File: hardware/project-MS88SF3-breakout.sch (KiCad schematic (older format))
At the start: 27 parts, among them J1 Conn_02x05_Odd_Even, J2 S2B-PH-SM4-TB(LF)(SN), J3 USB4105-GF-A, J4 Conn_01x12_Male, J5 Conn_01x16_Male, U1 MS88SF3

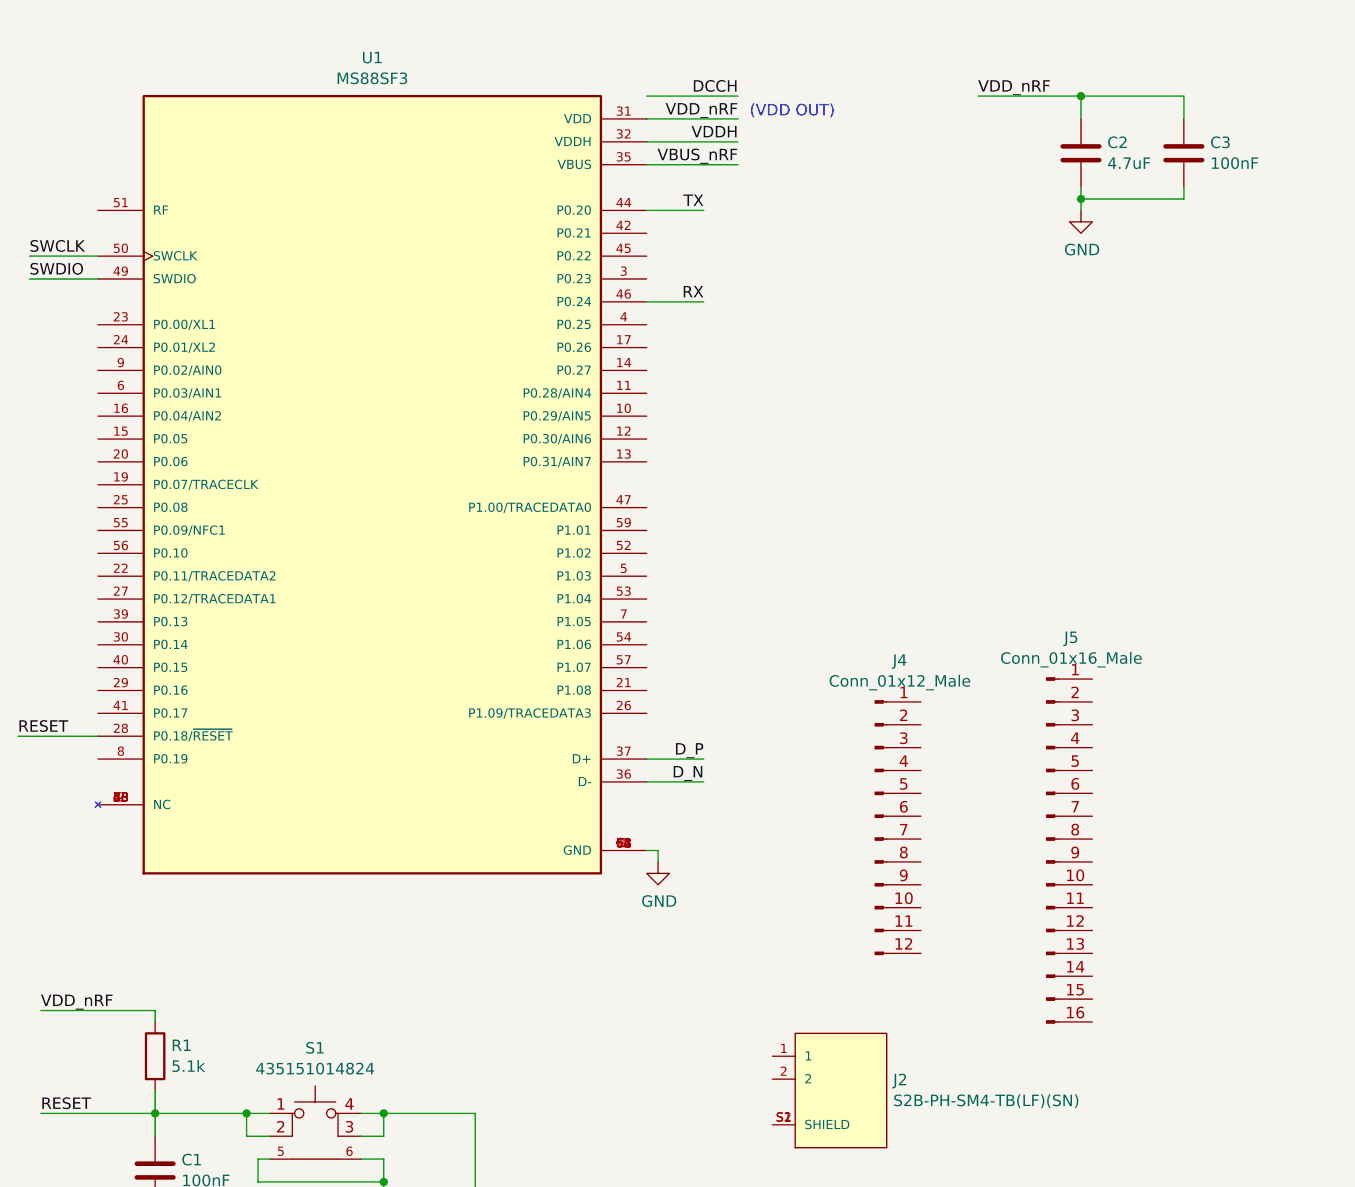
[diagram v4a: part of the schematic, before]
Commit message: Change the MS88SF3 module to the nRF52840
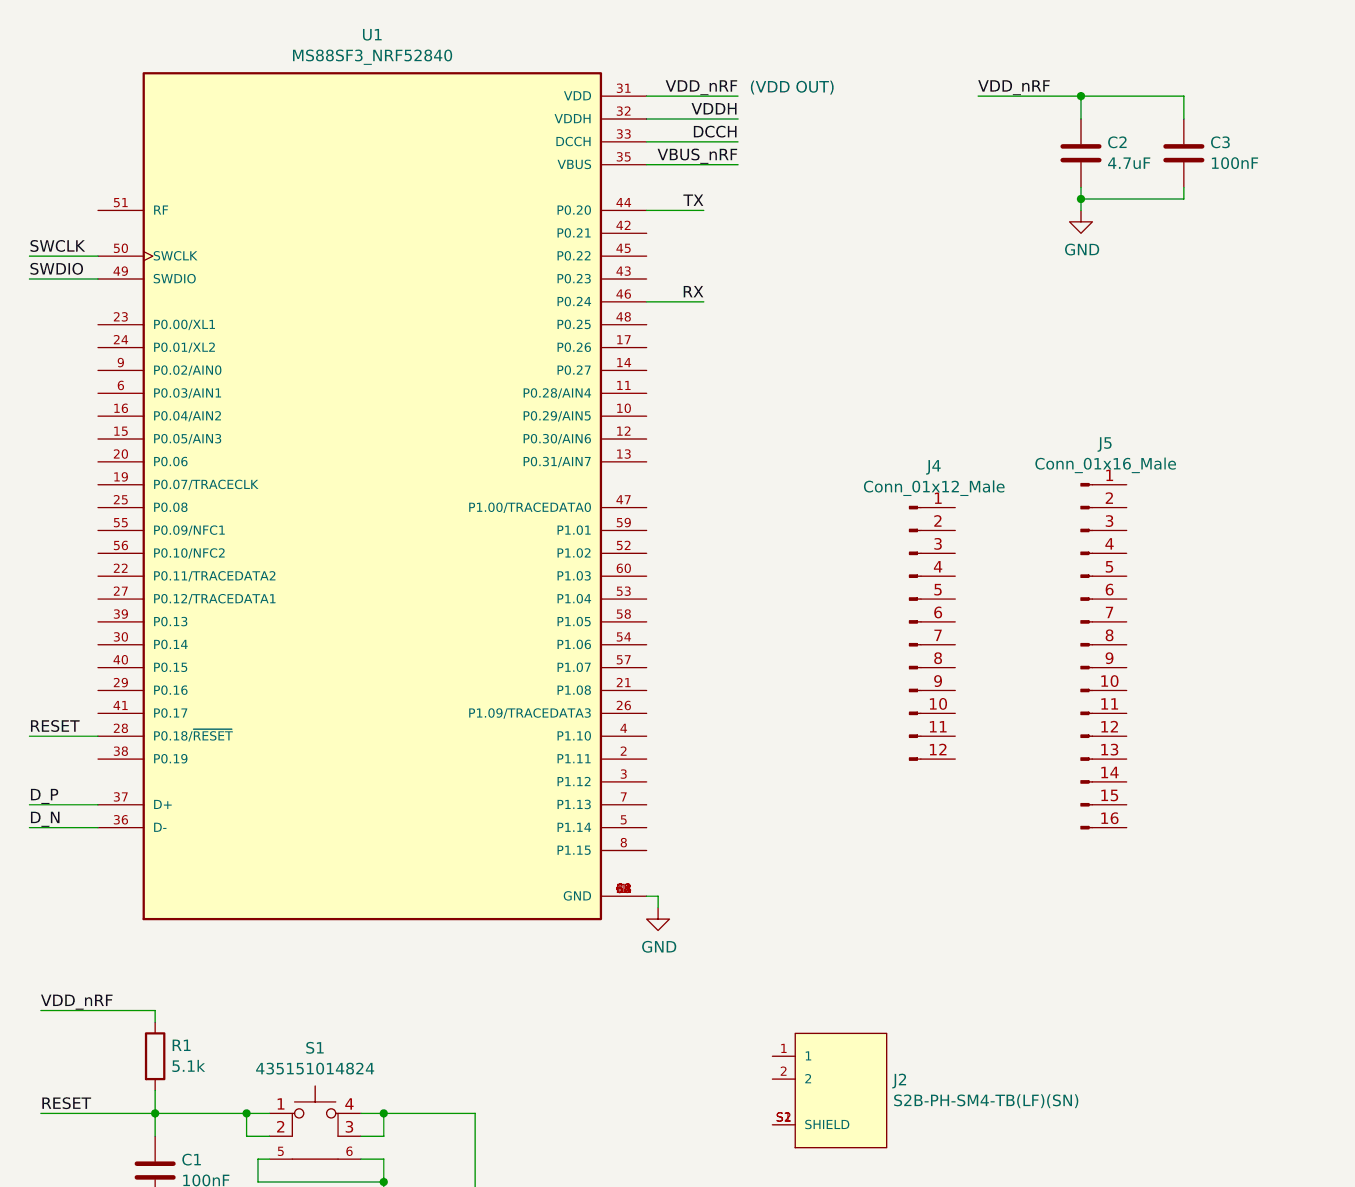
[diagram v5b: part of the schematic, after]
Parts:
- removed U1: MS88SF3, MODULE_MS88SF3, symbol MS88SF3:MS88SF3
- added U1: MS88SF3_NRF52840, MODULE_MS88SF3_NRF52840, symbol MS88SF3_NRF52840:MS88SF3_NRF52840
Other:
- moved on the sheet: J4, J5
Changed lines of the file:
@@
 $EndDescr
-$Comp
-L MS88SF3:MS88SF3 U1
-U 1 1 62BF0ECE
-P 2700 2850
-F 0 "U1" H 2700 4717 50  0000 C CNN
-F 1 "MS88SF3" H 2700 4626 50  0000 C CNN
-F 2 "MODULE_MS88SF3" H 2700 2850 50  0001 L BNN
-F 3 "" H 2700 2850 50  0001 L BNN
-F 4 "V1.0" H 2700 2850 50  0001 L BNN "PARTREV"
-F 5 "Minew" H 2700 2850 50  0001 L BNN "MANUFACTURER"
-F 6 "MS88SF3" H 2700 2850 50  0001 L BNN "SNAPEDA_PN"
-F 7 "2.15mm" H 2700 2850 50  0001 L BNN "MAXIMUM_PACKAGE_HEIGHT"
-F 8 "Manufacturer Recommendations" H 2700 2850 50  0001 L BNN "STANDARD"
-	1    2700 2850
-	1    0    0    -1
-$EndComp
 $Comp
 L power:GND #PWR01
@@
 $EndComp
 Wire Wire Line
-	3950 4500 3950 4450
-Wire Wire Line
-	3950 4450 3900 4450
+	3950 4700 3950 4650
+Wire Wire Line
+	3950 4650 3900 4650
 $Comp
 L USB4105-GF-A:USB4105-GF-A J3
@@
 $EndComp
 Wire Wire Line
-	1150 3950 1500 3950
-Text Label 1150 3950 0    50   ~ 0
+	1200 3950 1500 3950
+Text Label 1200 3950 0    50   ~ 0
 RESET
 Text Label 1250 5600 0    50   ~ 0
@@
 L Connector:Conn_01x12_Male J4
 U 1 1 6309BC95
-P 4900 4300
-F 0 "J4" H 5008 4981 50  0000 C CNN
-F 1 "Conn_01x12_Male" H 5008 4890 50  0000 C CNN
-F 2 "Connector_PinHeader_2.54mm:PinHeader_1x12_P2.54mm_Vertical" H 4900 4300 50  0001 C CNN
-F 3 "~" H 4900 4300 50  0001 C CNN
-	1    4900 4300
+P 5050 3450
+F 0 "J4" H 5158 4131 50  0000 C CNN
+F 1 "Conn_01x12_Male" H 5158 4040 50  0000 C CNN
+F 2 "Connector_PinHeader_2.54mm:PinHeader_1x12_P2.54mm_Vertical" H 5050 3450 50  0001 C CNN
+F 3 "~" H 5050 3450 50  0001 C CNN
+	1    5050 3450
 	1    0    0    -1
 $EndComp
@@
 L Connector:Conn_01x16_Male J5
 U 1 1 6309C92F
-P 5650 4400
-F 0 "J5" H 5758 5281 50  0000 C CNN
-F 1 "Conn_01x16_Male" H 5758 5190 50  0000 C CNN
-F 2 "Connector_PinHeader_2.54mm:PinHeader_1x16_P2.54mm_Vertical" H 5650 4400 50  0001 C CNN
-F 3 "~" H 5650 4400 50  0001 C CNN
-	1    5650 4400
-	1    0    0    -1
-$EndComp
-Text Notes 4350 1250 0    50   ~ 0
+P 5800 3550
+F 0 "J5" H 5908 4431 50  0000 C CNN
+F 1 "Conn_01x16_Male" H 5908 4340 50  0000 C CNN
+F 2 "Connector_PinHeader_2.54mm:PinHeader_1x16_P2.54mm_Vertical" H 5800 3550 50  0001 C CNN
+F 3 "~" H 5800 3550 50  0001 C CNN
+	1    5800 3550
+	1    0    0    -1
+$EndComp
+Text Notes 4350 1150 0    50   ~ 0
 (VDD OUT)
 Text Label 1250 5150 0    50   ~ 0
@@
 L power:GND #PWR0104
 U 1 1 630E24BF
-P 3950 4500
-F 0 "#PWR0104" H 3950 4250 50  0001 C CNN
-F 1 "GND" H 3955 4327 50  0000 C CNN
-F 2 "" H 3950 4500 50  0001 C CNN
-F 3 "" H 3950 4500 50  0001 C CNN
-	1    3950 4500
+P 3950 4700
+F 0 "#PWR0104" H 3950 4450 50  0001 C CNN
+F 1 "GND" H 3955 4527 50  0000 C CNN
+F 2 "" H 3950 4700 50  0001 C CNN
+F 3 "" H 3950 4700 50  0001 C CNN
+	1    3950 4700
 	1    0    0    -1
 $EndComp
@@
 	1200 1850 1500 1850
 Wire Wire Line
+	4300 1150 3900 1150
+Wire Wire Line
 	4300 1250 3900 1250
-Wire Wire Line
-	4300 1350 3900 1350
-Text Label 4300 1350 2    50   ~ 0
+Text Label 4300 1250 2    50   ~ 0
 VDDH
 Text Label 4300 1450 2    50   ~ 0
@@
 Wire Wire Line
 	3900 1450 4300 1450
-Text Label 4300 1250 2    50   ~ 0
+Text Label 4300 1150 2    50   ~ 0
 VDD_nRF
-Text Label 4300 1150 2    50   ~ 0
+Text Label 4300 1350 2    50   ~ 0
 DCCH
 Wire Wire Line
-	3900 1150 4300 1150
+	3900 1350 4300 1350
 Text Label 8500 1300 0    50   ~ 0
 VDDH
@@
 	1    0    0    -1
 $EndComp
-Text Label 4150 4050 2    50   ~ 0
+Text Label 1200 4250 0    50   ~ 0
 D_P
-Text Label 4150 4150 2    50   ~ 0
+Text Label 1200 4350 0    50   ~ 0
 D_N
 Wire Wire Line
-	4150 4150 3900 4150
-Wire Wire Line
-	4150 4050 3900 4050
+	1200 4350 1500 4350
+Wire Wire Line
+	1200 4250 1500 4250
 $Comp
 L 435151014824:435151014824 S1
@@
 Wire Wire Line
 	2750 5900 2750 6100
+$Comp
+L MS88SF3_NRF52840:MS88SF3_NRF52840 U1
+U 1 1 632BAEEC
+P 2700 2850
+F 0 "U1" H 2700 4817 50  0000 C CNN
+F 1 "MS88SF3_NRF52840" H 2700 4726 50  0000 C CNN
+F 2 "MODULE_MS88SF3_NRF52840" H 2700 2850 50  0001 L BNN
+F 3 "" H 2700 2850 50  0001 L BNN
+F 4 "2.15mm" H 2700 2850 50  0001 L BNN "MAXIMUM_PACKAGE_HEIGHT"
+F 5 "V1.1" H 2700 2850 50  0001 L BNN "PARTREV"
+F 6 "Minew" H 2700 2850 50  0001 L BNN "MANUFACTURER"
+F 7 "MS88SF3 NRF52840" H 2700 2850 50  0001 L BNN "SNAPEDA_PN"
+F 8 "Manufacturer Recommendations" H 2700 2850 50  0001 L BNN "STANDARD"
+	1    2700 2850
+	1    0    0    -1
+$EndComp
 $EndSCHEMATC

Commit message: Everything connected
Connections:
- net DCCH: now also L1.2; no longer L1.1
- net GND: now also J1.3 (Pin_3), J1.5 (Pin_5), J2.2, J2.S1 (SHIELD), J2.S2 (SHIELD), J5.13 (Pin_13)
- net RESET: now also J5.16 (Pin_16)
- net RX: now also J1.8 (Pin_8), J5.4 (Pin_4)
- net SWCLK: now also J1.4 (Pin_4)
- net SWDIO: now also J1.2 (Pin_2)
- net TX: now also J1.6 (Pin_6), J5.3 (Pin_3)
- net VBUS: now also J4.10 (Pin_10)
- net VDD_nRF: now also J2.1, J4.12 (Pin_12), J5.14 (Pin_14), J5.15 (Pin_15), L1.1; no longer L1.2
- net P1.10: now reaches J4.1 (Pin_1)
- net P1.10: now also U1.4 (P1.10)
- net P1.14: now reaches J4.2 (Pin_2)
- net P1.14: now also U1.5 (P1.14)
- net AIN1: now reaches J4.3 (Pin_3)
- net P1.13: now reaches J4.4 (Pin_4)
- net P1.13: now also U1.7 (P1.13)
- net P1.15: now reaches J4.5 (Pin_5)
- net P1.15: now also U1.8 (P1.15)
- net AIN0: now reaches J4.6 (Pin_6)
- net AIN0: now also U1.9 (P0.02/AIN0)
- net AIN5: now reaches J4.7 (Pin_7)
- net AIN5: now also U1.10 (P0.29/AIN5)
- net AIN3: now reaches J4.8 (Pin_8)
- net AIN3: now also U1.15 (P0.05/AIN3)
- net AIN2: now reaches J4.9 (Pin_9)
- net AIN2: now also U1.16 (P0.04/AIN2)
- net NFC1: now reaches J5.1 (Pin_1)
- net NFC1: now also U1.55 (P0.09/NFC1)
- net P0.15: now reaches J5.10 (Pin_10)
- net P0.15: now also U1.40 (P0.15)
- net P0.13: now reaches J5.11 (Pin_11)
- net P0.13: now also U1.39 (P0.13)
- net P0.19: now reaches J5.12 (Pin_12)
- net P0.19: now also U1.38 (P0.19)
- net NFC2: now reaches J5.2 (Pin_2)
- net NFC2: now also U1.56 (P0.10/NFC2)
- net P0.25: now reaches J5.5 (Pin_5)
- net P0.25: now also U1.48 (P0.25)
- net P0.22: now reaches J5.6 (Pin_6)
- net P0.22: now also U1.45 (P0.22)
- net P0.23: now reaches J5.7 (Pin_7)
- net P0.23: now also U1.43 (P0.23)
- net P0.21: now reaches J5.8 (Pin_8)
- net P0.21: now also U1.42 (P0.21)
- net P0.17: now reaches J5.9 (Pin_9)
- net P0.17: now also U1.41 (P0.17)
- net P1.11: now reaches U1.2 (P1.11)
- net P1.12: now reaches U1.3 (P1.12)
- no-connect marks 2 -> 6
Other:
- note added: "PCA10059\nRevision: 2.0.0\n17.09.2020"
- moved on the sheet: C2, C3, C4, C5, H1, H2, H3, H4, J1, J3, J4, J5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

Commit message: Half routing done
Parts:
- removed C3: 100nF, Capacitor_SMD:C_0603_1608Metric, symbol Device:C
- added C6: 4.7uF, Capacitor_SMD:C_0805_2012Metric, symbol Device:C
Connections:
- net GND: now also C6.2
- net VBUS_nRF: now also C6.1
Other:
- moved on the sheet: C2, JP1, JP2, L1, R3
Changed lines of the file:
@@
 L Device:R R3
 U 1 1 630309A2
-P 7750 1450
-F 0 "R3" V 7957 1450 50  0000 C CNN
-F 1 "4.7" V 7866 1450 50  0000 C CNN
-F 2 "Resistor_SMD:R_0603_1608Metric" V 7680 1450 50  0001 C CNN
-F 3 "~" H 7750 1450 50  0001 C CNN
-	1    7750 1450
+P 8800 1450
+F 0 "R3" V 9007 1450 50  0000 C CNN
+F 1 "4.7" V 8916 1450 50  0000 C CNN
+F 2 "Resistor_SMD:R_0603_1608Metric" V 8730 1450 50  0001 C CNN
+F 3 "~" H 8800 1450 50  0001 C CNN
+	1    8800 1450
 	0    -1   -1   0
 $EndComp
@@
 $EndComp
 $Comp
-L Device:C C3
-U 1 1 63088C20
-P 6450 1200
-F 0 "C3" H 6565 1246 50  0000 L CNN
-F 1 "100nF" H 6565 1155 50  0000 L CNN
-F 2 "Capacitor_SMD:C_0603_1608Metric" H 6488 1050 50  0001 C CNN
-F 3 "~" H 6450 1200 50  0001 C CNN
-	1    6450 1200
-	1    0    0    -1
-$EndComp
-$Comp
 L Device:C C2
 U 1 1 63088C26
-P 6000 1200
-F 0 "C2" H 6115 1246 50  0000 L CNN
-F 1 "4.7uF" H 6115 1155 50  0000 L CNN
-F 2 "Capacitor_SMD:C_0805_2012Metric" H 6038 1050 50  0001 C CNN
-F 3 "~" H 6000 1200 50  0001 C CNN
-	1    6000 1200
+P 7750 1150
+F 0 "C2" H 7865 1196 50  0000 L CNN
+F 1 "4.7uF" H 7865 1105 50  0000 L CNN
+F 2 "Capacitor_SMD:C_0805_2012Metric" H 7788 1000 50  0001 C CNN
+F 3 "~" H 7750 1150 50  0001 C CNN
+	1    7750 1150
 	1    0    0    -1
 $EndComp
@@
 Wire Wire Line
 	1750 6000 1750 6100
-Text Label 5550 950  0    50   ~ 0
-VDD_nRF
-Wire Wire Line
-	5550 950  6000 950
-Wire Wire Line
-	6000 950  6000 1050
-Wire Wire Line
-	6000 950  6450 950
-Wire Wire Line
-	6450 950  6450 1050
-Connection ~ 6000 950
 $Comp
 L power:GND #PWR0105
 U 1 1 630EDA38
-P 6000 1450
-F 0 "#PWR0105" H 6000 1200 50  0001 C CNN
-F 1 "GND" H 6005 1277 50  0000 C CNN
-F 2 "" H 6000 1450 50  0001 C CNN
-F 3 "" H 6000 1450 50  0001 C CNN
-	1    6000 1450
-	1    0    0    -1
-$EndComp
-Wire Wire Line
-	6000 1350 6000 1400
-Wire Wire Line
-	6450 1350 6450 1400
-Wire Wire Line
-	6450 1400 6000 1400
-Connection ~ 6000 1400
-Wire Wire Line
-	6000 1400 6000 1450
+P 7750 1350
+F 0 "#PWR0105" H 7750 1100 50  0001 C CNN
+F 1 "GND" H 7755 1177 50  0000 C CNN
+F 2 "" H 7750 1350 50  0001 C CNN
+F 3 "" H 7750 1350 50  0001 C CNN
+	1    7750 1350
+	1    0    0    -1
+$EndComp
 Text Label 9850 5550 0    50   ~ 0
 VBUS
@@
 Wire Wire Line
 	3900 1350 4300 1350
-Text Label 10600 1300 2    50   ~ 0
+Text Label 10700 1300 2    50   ~ 0
 VDDH
-Text Label 10600 900  2    50   ~ 0
+Text Label 10700 900  2    50   ~ 0
 VDD_nRF
 Wire Wire Line
-	8850 950  8850 900
-Wire Wire Line
-	8850 1450 8750 1450
-Wire Wire Line
-	8850 1250 8850 1300
-Wire Wire Line
-	10600 1300 8850 1300
-Text Label 7950 1200 0    50   ~ 0
+	9650 950  9650 900
+Wire Wire Line
+	9650 1450 9550 1450
+Wire Wire Line
+	9650 1250 9650 1300
+Wire Wire Line
+	10700 1300 9650 1300
+Text Label 8750 1100 0    50   ~ 0
 VBUS_nRF
 $Comp
 L Jumper:SolderJumper_2_Open JP2
 U 1 1 63036BBA
-P 8850 1100
-F 0 "JP2" V 8850 1168 50  0000 L CNN
-F 1 "SolderJumper_2_Open" V 8895 1168 50  0001 L CNN
-F 2 "Jumper:SolderJumper-2_P1.3mm_Open_RoundedPad1.0x1.5mm" H 8850 1100 50  0001 C CNN
-F 3 "~" H 8850 1100 50  0001 C CNN
-	1    8850 1100
+P 9650 1100
+F 0 "JP2" V 9650 1168 50  0000 L CNN
+F 1 "SolderJumper_2_Open" V 9695 1168 50  0001 L CNN
+F 2 "Jumper:SolderJumper-2_P1.3mm_Open_RoundedPad1.0x1.5mm" H 9650 1100 50  0001 C CNN
+F 3 "~" H 9650 1100 50  0001 C CNN
+	1    9650 1100
 	0    1    1    0
 $EndComp
@@
 L Jumper:SolderJumper_2_Bridged JP1
 U 1 1 63036196
-P 8600 1450
-F 0 "JP1" H 8600 1563 50  0000 C CNN
-F 1 "SolderJumper_2_Bridged" H 8600 1564 50  0001 C CNN
-F 2 "Jumper:SolderJumper-2_P1.3mm_Bridged_RoundedPad1.0x1.5mm" H 8600 1450 50  0001 C CNN
-F 3 "~" H 8600 1450 50  0001 C CNN
-	1    8600 1450
-	1    0    0    -1
-$EndComp
-Wire Wire Line
-	9950 1150 10050 1150
-Text Label 10600 1150 2    50   ~ 0
+P 9400 1450
+F 0 "JP1" H 9400 1563 50  0000 C CNN
+F 1 "SolderJumper_2_Bridged" H 9400 1564 50  0001 C CNN
+F 2 "Jumper:SolderJumper-2_P1.3mm_Bridged_RoundedPad1.0x1.5mm" H 9400 1450 50  0001 C CNN
+F 3 "~" H 9400 1450 50  0001 C CNN
+	1    9400 1450
+	1    0    0    -1
+$EndComp
+Wire Wire Line
+	10050 1150 10150 1150
+Text Label 10700 1150 2    50   ~ 0
 DCCH
 Wire Wire Line
-	10600 1150 10350 1150
+	10700 1150 10450 1150
 $Comp
 L Device:L L1
 U 1 1 630235F3
-P 10200 1150
-F 0 "L1" V 10390 1150 50  0000 C CNN
-F 1 "10uH" V 10299 1150 50  0000 C CNN
-F 2 "Inductor_SMD:L_0603_1608Metric" H 10200 1150 50  0001 C CNN
-F 3 "~" H 10200 1150 50  0001 C CNN
-	1    10200 1150
+P 10300 1150
+F 0 "L1" V 10490 1150 50  0000 C CNN
+F 1 "10uH" V 10399 1150 50  0000 C CNN
+F 2 "Inductor_SMD:L_0603_1608Metric" H 10300 1150 50  0001 C CNN
+F 3 "~" H 10300 1150 50  0001 C CNN
+	1    10300 1150
 	0    -1   -1   0
 $EndComp
@@
 $EndComp
 Wire Wire Line
-	10600 900  9950 900
-Wire Wire Line
-	9950 1150 9950 900
-Connection ~ 9950 900
-Wire Wire Line
-	9950 900  8850 900
+	10700 900  10050 900
+Wire Wire Line
+	10050 1150 10050 900
+Connection ~ 10050 900
+Wire Wire Line
+	10050 900  9650 900
 Wire Wire Line
 	9700 4000 9400 4000
-Text Label 7150 1200 0    50   ~ 0
+Text Label 8200 1100 0    50   ~ 0
 VBUS
 Wire Wire Line
-	7150 1200 7450 1200
-Connection ~ 8850 1300
-Wire Wire Line
-	7450 1200 7450 1450
-Wire Wire Line
-	7450 1450 7600 1450
-Wire Wire Line
-	7900 1450 8350 1450
-Wire Wire Line
-	7950 1200 8350 1200
-Wire Wire Line
-	8350 1200 8350 1450
-Connection ~ 8350 1450
-Wire Wire Line
-	8350 1450 8450 1450
-Text Notes 10000 1700 0    50   ~ 0
+	8200 1100 8500 1100
+Connection ~ 9650 1300
+Wire Wire Line
+	8500 1100 8500 1450
+Wire Wire Line
+	8500 1450 8650 1450
+Wire Wire Line
+	8950 1450 9150 1450
+Wire Wire Line
+	8750 1100 9150 1100
+Wire Wire Line
+	9150 1100 9150 1450
+Connection ~ 9150 1450
+Wire Wire Line
+	9150 1450 9250 1450
+Text Notes 10100 1700 0    50   ~ 0
 PCA10059\nRevision: 2.0.0\n17.09.2020
 Wire Wire Line
-	8850 1300 8850 1450
-Wire Wire Line
-	6850 900  8850 900
-Connection ~ 8850 900
-Text Label 6850 900  0    50   ~ 0
+	9650 1300 9650 1450
+Wire Wire Line
+	7250 900  7750 900
+Connection ~ 9650 900
+Text Label 7250 900  0    50   ~ 0
 VDD_nRF
 $Comp
@@
 Wire Wire Line
 	1150 4050 1500 4050
+$Comp
+L Device:C C6
+U 1 1 637D6BC6
+P 9150 1700
+F 0 "C6" H 9265 1746 50  0000 L CNN
+F 1 "4.7uF" H 9265 1655 50  0000 L CNN
+F 2 "Capacitor_SMD:C_0805_2012Metric" H 9188 1550 50  0001 C CNN
+F 3 "~" H 9150 1700 50  0001 C CNN
+	1    9150 1700
+	1    0    0    -1
+$EndComp
+$Comp
+L power:GND #PWR04
+U 1 1 637D6BD2
+P 9150 1900
+F 0 "#PWR04" H 9150 1650 50  0001 C CNN
+F 1 "GND" H 9155 1727 50  0000 C CNN
+F 2 "" H 9150 1900 50  0001 C CNN
+F 3 "" H 9150 1900 50  0001 C CNN
+	1    9150 1900
+	1    0    0    -1
+$EndComp
+Wire Wire Line
+	9150 1850 9150 1900
+Wire Wire Line
+	9150 1450 9150 1550
+Wire Wire Line
+	7750 1300 7750 1350
+Wire Wire Line
+	7750 900  7750 1000
+Connection ~ 7750 900
+Wire Wire Line
+	7750 900  9650 900
+$Comp
+L power:PWR_FLAG #FLG?
+U 1 1 6391DB45
+P 7750 900
+F 0 "#FLG?" H 7750 975 50  0001 C CNN
+F 1 "PWR_FLAG" H 7750 1073 50  0000 C CNN
+F 2 "" H 7750 900 50  0001 C CNN
+F 3 "~" H 7750 900 50  0001 C CNN
+	1    7750 900
+	1    0    0    -1
+$EndComp
 $EndSCHEMATC

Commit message: USB route
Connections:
- net AIN1: now also U1.6 (P0.03/AIN1)
- net RX: now also J5.3 (Pin_3); no longer J5.4 (Pin_4)
- net TX: now also J5.4 (Pin_4); no longer J5.3 (Pin_3)
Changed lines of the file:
@@
 Wire Wire Line
 	6200 4050 5850 4050
+Text Label 5850 3150 0    50   ~ 0
+TX
 Text Label 5850 3050 0    50   ~ 0
-TX
-Text Label 5850 3150 0    50   ~ 0
 RX
 Wire Wire Line
@@
 	7750 900  9650 900
 $Comp
-L power:PWR_FLAG #FLG?
+L power:PWR_FLAG #FLG0101
 U 1 1 6391DB45
 P 7750 900
-F 0 "#FLG?" H 7750 975 50  0001 C CNN
+F 0 "#FLG0101" H 7750 975 50  0001 C CNN
 F 1 "PWR_FLAG" H 7750 1073 50  0000 C CNN
 F 2 "" H 7750 900 50  0001 C CNN
@@
 	1    0    0    -1
 $EndComp
+Text Label 1150 2450 0    50   ~ 0
+AIN1
+Wire Wire Line
+	1150 2450 1500 2450
 $EndSCHEMATC
